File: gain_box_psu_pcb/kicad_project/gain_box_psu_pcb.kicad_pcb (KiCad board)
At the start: 2 copper layers, 170 x 85 mm, 78 parts, among them J1 Conn_01x02, J2 Conn_01x04, J3 Conn_01x03, J4 Conn_01x02, J5 Conn_01x02, J6 AVR-UPDI-6, K1 J107F1CS2012VDC.80, K2 J104D2C12VDC.36S, Q1 AO3400A, Q2 AO3400A, Q3 AO3400A, T1 70042K, U1 LM7809, U2 LM7909, U3 78L05, U4 140817141310, U5 ATtiny412-SS

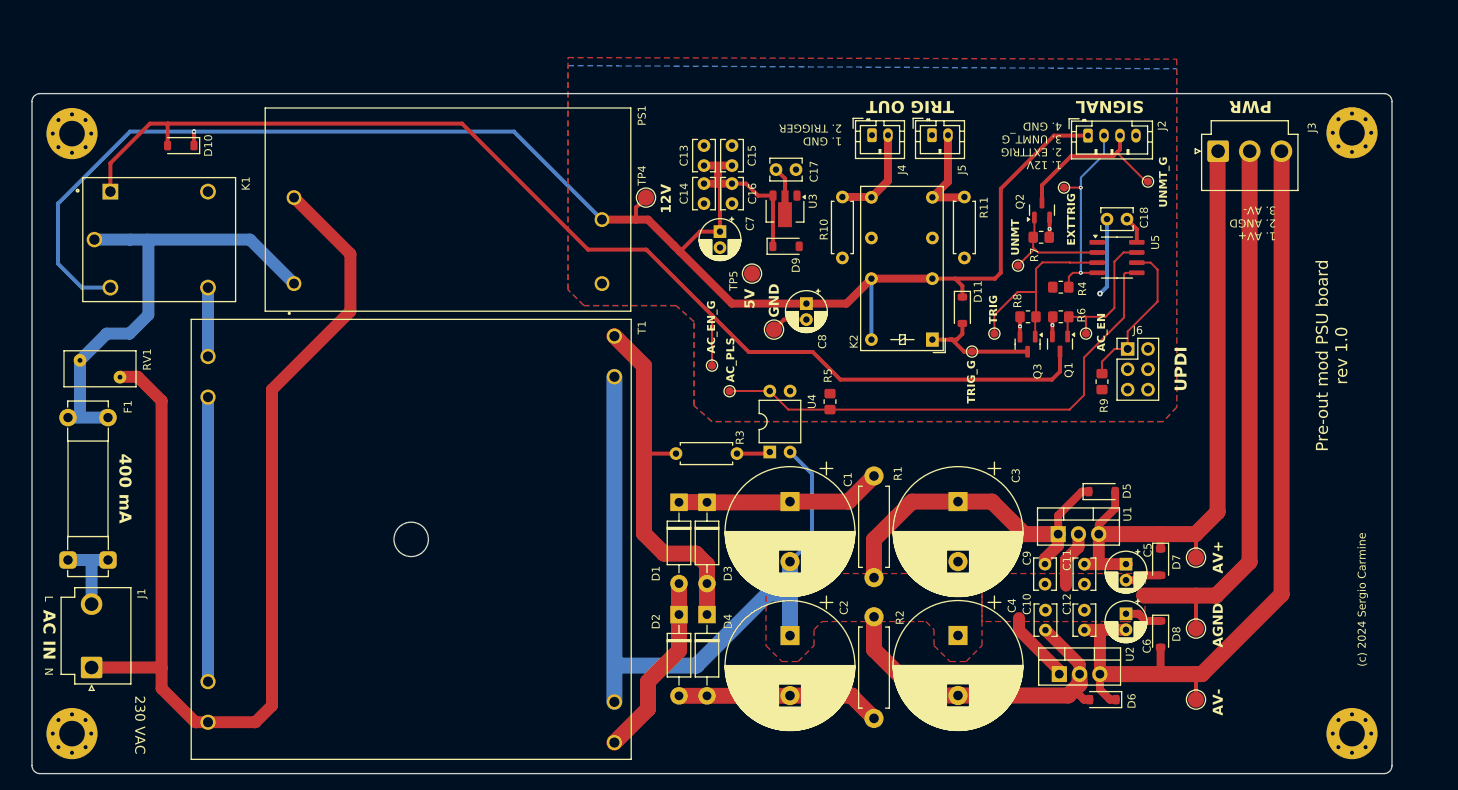
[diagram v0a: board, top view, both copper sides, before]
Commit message: Shorten PSU PCB
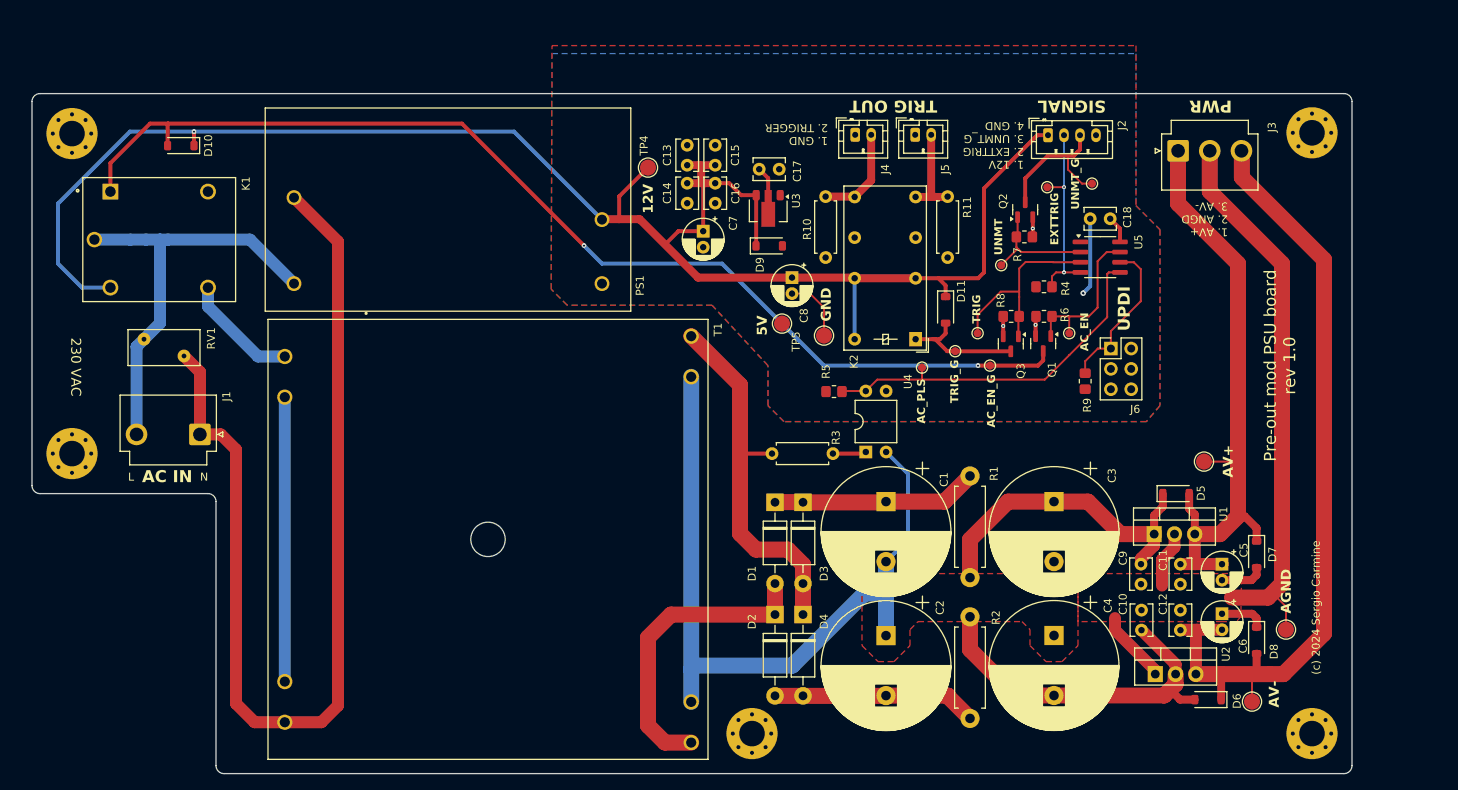
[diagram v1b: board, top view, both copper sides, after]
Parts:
- removed F1: 400 mA, Fuse:Fuseholder_Clip-5x20mm_Bel_FC-203-22_Lateral_P17.80x5.00mm_D1.17mm_Horizontal
- added H5: MountingHole_Pad, MountingHole:MountingHole_3.2mm_M3_Pad_Via, F.Cu at (148.0, 139.0)
- moved H3 35.0 mm to (63.0, 104.0)
- moved TP10 34.8 mm to (177.8, 93.0)
- moved J1 32.1 mm to (79.0, 101.6), turned to 180 degrees
- moved TP13 24.2 mm to (169.2, 93.2)
- moved D6 13.2 mm to (205.0, 134.8)
- moved TP1 12.0 mm to (204.5, 105.0)
- moved D7 12.0 mm to (211.1, 116.6)
- moved D8 12.0 mm to (211.1, 127.3)
- moved C1 12.0 mm to (164.8, 110.0)
- moved C10 12.0 mm to (196.7, 123.6)
- moved C11 12.0 mm to (201.6, 117.8)
- moved C12 12.0 mm to (201.6, 123.6)
- moved C2 12.0 mm to (164.8, 126.8)
- moved C3 12.0 mm to (185.8, 110.0)
- moved C4 12.0 mm to (185.8, 126.7)
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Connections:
- J1 pad 2: Net-(J1-Pin_2) -> AC_L
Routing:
- net AC_PULSE: track 64.9 -> 45.6 mm
- net Net-(D1-A): track 23.2 -> 38.2 mm
- net Net-(J1-Pin_2): track 10.6 -> 0.00 mm
- net AC_EN_G: track 149.5 -> 138.9 mm, vias 0 -> 2
- net AC_N: track 138.1 -> 128.0 mm
- net AC_L: track 59.9 -> 52.8 mm
- net AC_L_SW: track 8.61 -> 14.5 mm
- net AGND: track 187.2 -> 191.9 mm
- net GND: track 20.4 -> 24.1 mm
- net +12V: track 219.9 -> 216.4 mm
- net AV+: track 81.5 -> 79.5 mm
- net Net-(D5-K): track 43.3 -> 41.4 mm
- net UNMUTE_G: track 20.9 -> 19.3 mm
- net EXTTRIG: track 25.5 -> 24.3 mm
- net Net-(D6-A): track 43.5 -> 44.6 mm
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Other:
- board size 170 x 85 mm -> 165 x 85 mm
- board text removed: "400 mA"

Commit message: Update PSU PCB
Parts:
- added G***: LOGO, project_lib:GND_Symbol, F.Cu at (65.0, 91.0)
- added H6: Screw_Terminal_01x01, project_lib:KEYSTONE_7760, F.Cu at (63.4, 72.0)
- moved T1 16.6 mm to (131.2, 111.0)
- moved H5 16.6 mm to (164.2, 135.3)
- moved TP6 14.5 mm to (147.4, 78.3)
- moved C8 14.5 mm to (167.0, 78.2)
- moved TP5 13.6 mm to (157.7, 75.5)
- moved U3 13.3 mm to (161.1, 66.4)
- moved C17 13.3 mm to (162.5, 61.2)
- moved D9 13.3 mm to (161.3, 70.8)
- moved D2 12.6 mm to (162.0, 118.3)
- moved D4 12.6 mm to (165.5, 118.3)
- moved D1 12.6 mm to (162.0, 104.2)
- moved D3 12.6 mm to (165.5, 104.2)
- moved R10 12.0 mm to (168.0, 74.3)
- moved R3 11.8 mm to (161.7, 100.0)
- moved D11 11.8 mm to (183.4, 82.3)
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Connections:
- H2 pad 1: unconnected-(H2-Pad1)_7 -> Earth
- H3 pad 1: unconnected-(H3-Pad1)_4 -> Earth
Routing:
- net AGND: track 191.9 -> 183.0 mm
- net Net-(D1-A): track 38.2 -> 29.7 mm
- net AC_N: track 128.0 -> 135.7 mm
- net AC_L_SW: track 14.5 -> 19.5 mm
- net AC_SENSE: track 46.9 -> 50.8 mm
- net Earth: track 0.00 -> 1.53 mm
- net TGO1: track 12.2 -> 13.3 mm
- net Net-(D1-K): track 25.9 -> 26.8 mm
- net Net-(D2-A): track 25.6 -> 26.5 mm
- net GND: track 24.1 -> 23.3 mm
- added copper zone on F.Cu, net Earth
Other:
- board size 165 x 85 mm -> 175 x 85 mm

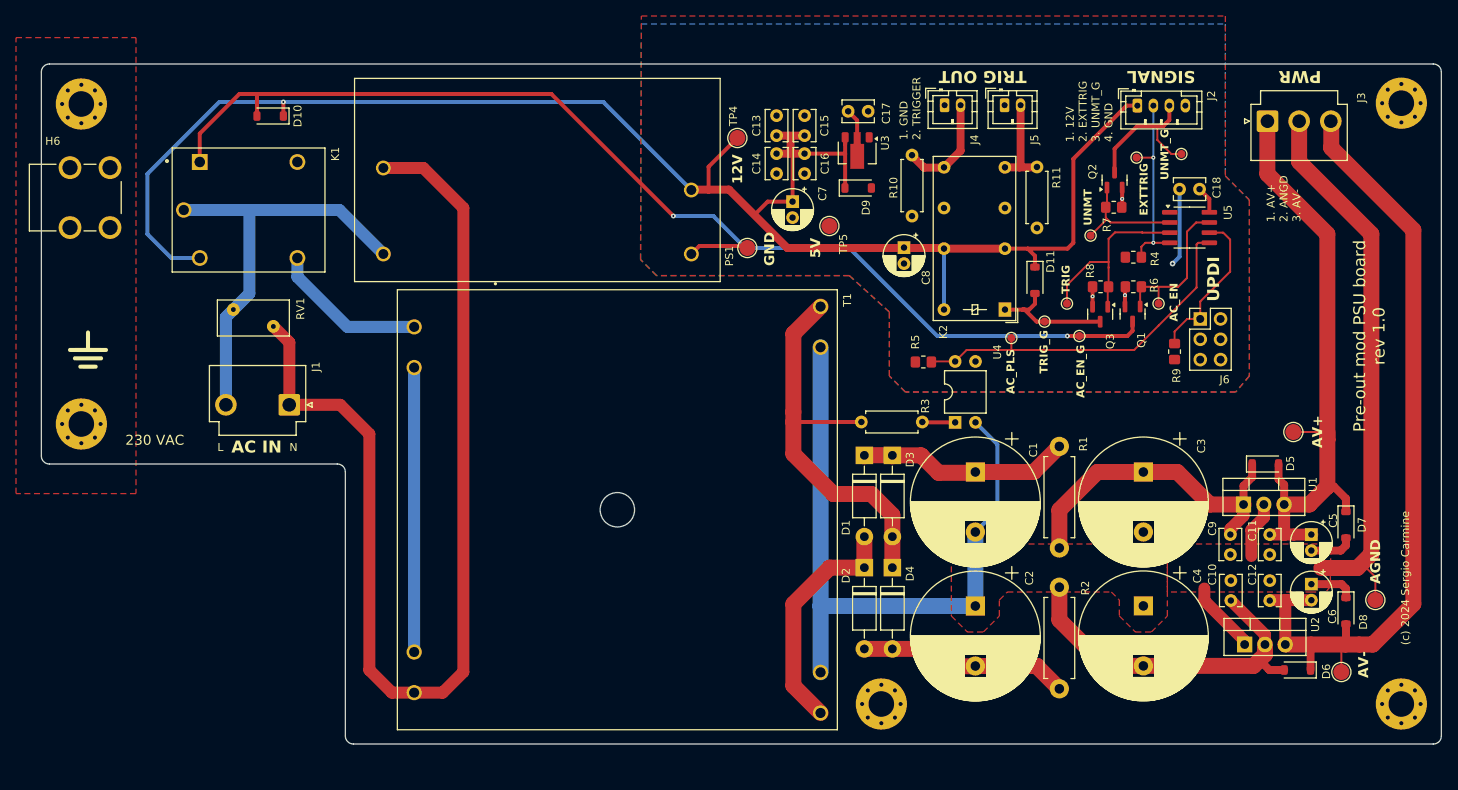
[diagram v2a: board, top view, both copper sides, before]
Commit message: New main PSU caps
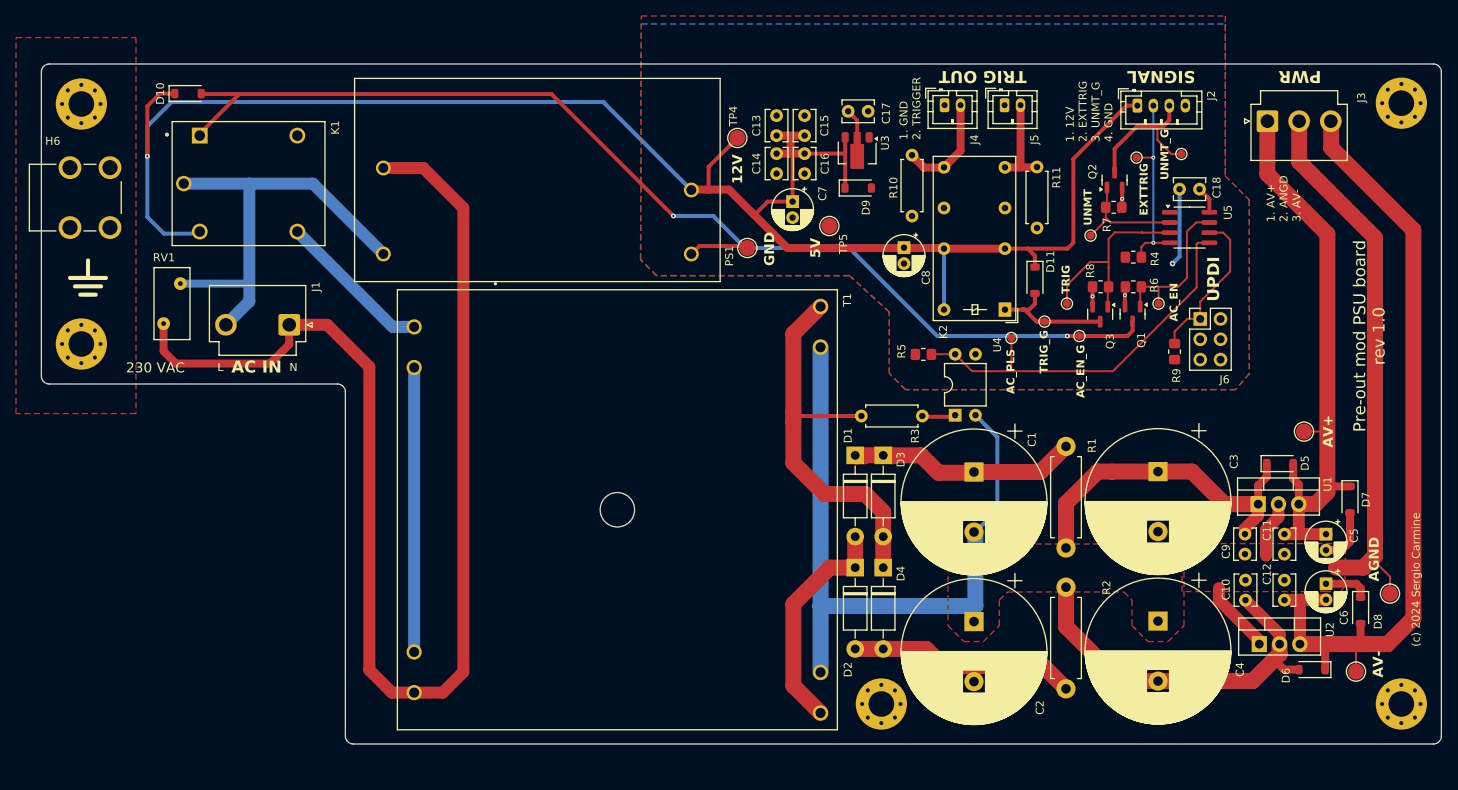
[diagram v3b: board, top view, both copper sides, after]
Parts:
- C1, C2, C3, C4: footprint Capacitor_THT:CP_Radial_D16.0mm_P7.50mm -> Capacitor_THT:CP_Radial_D18.0mm_P7.50mm
- moved D10 10.6 mm to (77.5, 59.0), turned to 0 degrees
- moved H3 10.0 mm to (64.2, 90.3)
- moved J1 10.0 mm to (90.2, 87.9)
- moved G*** 9.00 mm to (65.0, 82.0)
- moved RV1 7.37 mm to (76.5, 82.8), turned to -90 degrees
- moved K1 3.30 mm to (85.1, 70.2)
- moved D7 3.19 mm to (222.8, 109.8)
- moved C4 2.64 mm to (198.8, 124.9)
- moved TP2 2.00 mm to (227.8, 121.5)
- moved C2 1.96 mm to (175.8, 125.0)
- moved C11 1.83 mm to (214.6, 114.1)
- moved C12 1.83 mm to (214.6, 119.8)
- moved C5 1.83 mm to (219.8, 114.1)
- moved D6 1.83 mm to (218.0, 131.0)
- moved TP3 1.83 mm to (223.5, 131.2)
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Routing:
- net AC_N: track 135.7 -> 157.4 mm
- net +12V: track 216.6 -> 226.2 mm
- net AV+: track 79.5 -> 73.9 mm
- net AC_PULSE: track 45.6 -> 49.5 mm
- net Net-(D6-A): track 44.6 -> 48.0 mm
- net Net-(D1-K): track 26.8 -> 29.9 mm
- net AC_L: track 52.8 -> 55.8 mm
- net Net-(D2-A): track 26.5 -> 28.4 mm
- net Net-(D5-K): track 41.4 -> 42.9 mm
- net AC_EN_G: track 138.9 -> 137.7 mm
- net Earth: track 1.53 -> 0.35 mm
- net Net-(D1-A): track 29.7 -> 28.5 mm
- net AGND: track 183.0 -> 184.1 mm
- net AV-: track 103.3 -> 102.5 mm
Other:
- outline, holes or cut-outs redrawn

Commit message: Sent to production
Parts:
- T1: value 70042K -> 70023K; footprint project_lib:XFMR_70042K -> project_lib:TRANS_Talema_70023K
- U1: value LM7809 -> LM7812
- U2: value LM7909 -> LM7912
- moved R3 11.5 mm to (157.2, 88.7), turned to -90 degrees
- moved TP13 9.33 mm to (171.8, 93.0)
- moved U4 8.71 mm to (164.7, 100.0)
- moved H5 5.00 mm to (159.2, 135.3)
- moved R5 4.97 mm to (165.8, 88.2), turned to 0 degrees
- moved D1 3.40 mm to (157.5, 104.2)
- moved D2 3.40 mm to (157.5, 118.3)
- moved D3 3.40 mm to (161.0, 104.2)
- moved D4 3.40 mm to (161.0, 118.3)
- moved C8 2.93 mm to (166.0, 81.0)
- moved C1 2.83 mm to (172.9, 106.3)
- moved C2 2.83 mm to (172.9, 125.0)
- moved C3 2.83 mm to (195.9, 106.2)
- moved C4 2.83 mm to (195.9, 124.9)
- moved R1 2.83 mm to (184.4, 103.1)
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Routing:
- net AC_PULSE: track 49.5 -> 58.4 mm
- net Net-(R3-Pad2): track 4.19 -> 10.3 mm
- net AC_N: track 157.4 -> 152.0 mm
- net AC_SENSE: track 50.6 -> 45.2 mm
- net Net-(T1-Pad4): track 35.6 -> 30.5 mm
- net Net-(D6-A): track 48.0 -> 50.8 mm
- net Net-(D5-K): track 42.9 -> 45.7 mm
- net AGND: track 184.1 -> 181.4 mm
- net +12V: track 226.2 -> 228.9 mm
- net AC_L_SW: track 19.5 -> 21.5 mm
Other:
- board text added: "(c) 2025 Sergio Carmine"
- board text added: "1. AV+ 2. AGND 3. AV-"
- board text removed: "(c) 2024 Sergio Carmine"
- board text removed: "1. AV+ 2. ANGD 3. AV-"
